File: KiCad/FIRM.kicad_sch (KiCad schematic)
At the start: 56 parts, among them J1 Conn_01x04_Pin, J2 USB_A, J3 Micro_SD_Card_Det2, Q1 AO3401A, U1 STM32F405RGTx, U2 LM2596S-3.3, U6 AP2112K-3.3, U7 W25Q128JVS, X2 32.768khz, Y1 12mhz

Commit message: test
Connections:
- net USB_D+ is gone; now on net VBUS: J2.3 (D+), U1.45 (PA12)
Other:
- moved on the sheet: C22, C23, C24, D1, Q1, R8, R9, U6

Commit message: update with drive
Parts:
- removed J2: USB_A, symbol Connector:USB_A
- removed U2: LM2596S-3.3, Package_TO_SOT_SMD:TO-263-5_TabPin3, symbol Regulator_Switching:LM2596S-3.3
- added J5: USB_C_Receptacle_USB2.0_16P, symbol Connector:USB_C_Receptacle_USB2.0_16P
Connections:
- net MISO is gone; now on net MISO2: U5.5 (SDO)
- net MOSI is gone; now on net MOSI2: U5.4 (SDI)
- net GND: now also J5.A1 (GND), J5.A12 (GND), J5.B1 (GND), J5.B12 (GND), J5.S1 (SHIELD)
- net USB_D-: now also J5.A7 (D-), J5.B7 (D-)
- net VBUS: now also J5.A4 (VBUS), J5.A9 (VBUS), J5.B4 (VBUS), J5.B9 (VBUS); no longer U1.45 (PA12)
- new net USB_D+: J5.A6 (D+), J5.B6 (D+), U1.45 (PA12)
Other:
- moved on the sheet: C22, C23, C24, D1, Q1, R8, R9, U6

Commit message: connector jst
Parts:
- added D5: LED, symbol Device:LED
- added R15: 2k2, symbol Device:R_Small
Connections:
- net +3.3V: now also R15.2
- net GND: now also D5.1 (K); no longer J1.3 (Pin_3), U1.49 (PA14)
- new net: D5.2 (A), R15.1
- new net SWCLK: J1.3 (Pin_3), U1.49 (PA14)
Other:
- moved on the sheet: J1

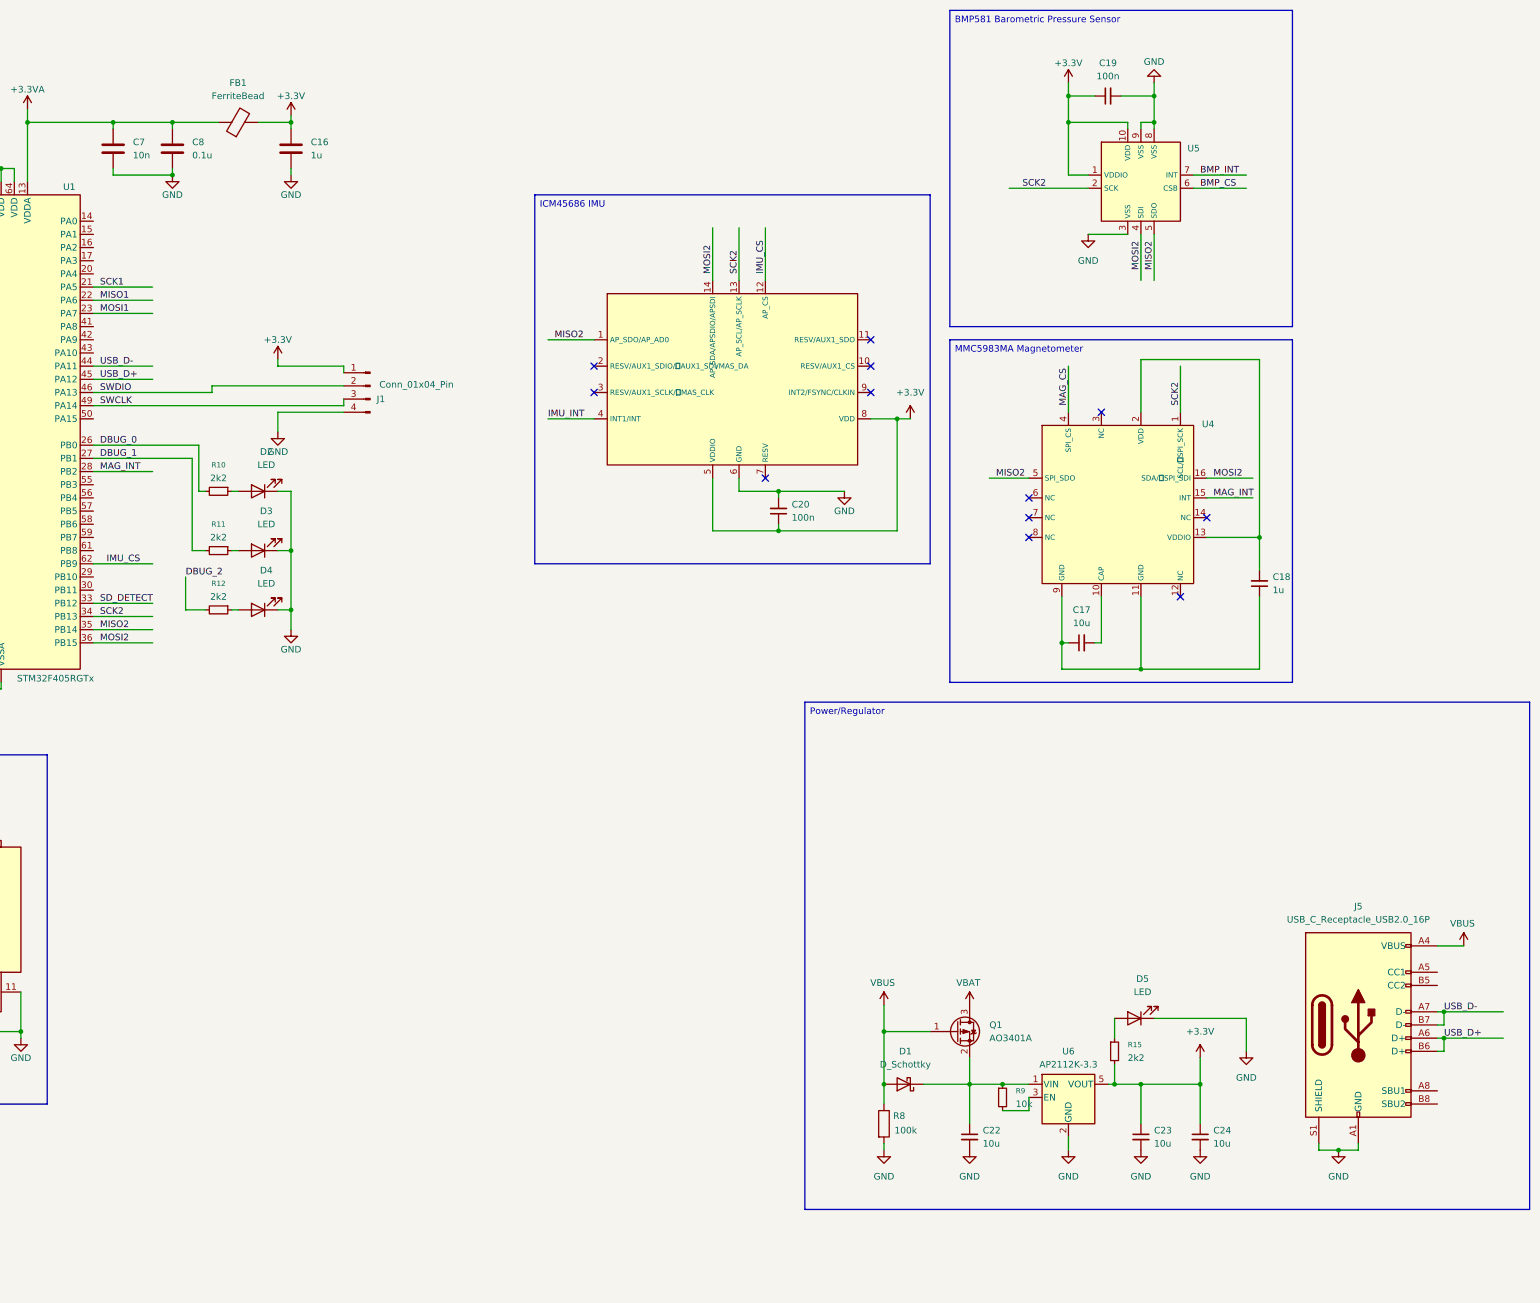
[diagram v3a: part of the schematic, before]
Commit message: Sensors Power/Decoupling and IMU/MMC Footprints
Fixed ICM, BMP, and MMC's power and decoupling. Added footprints for the MMC and ICM
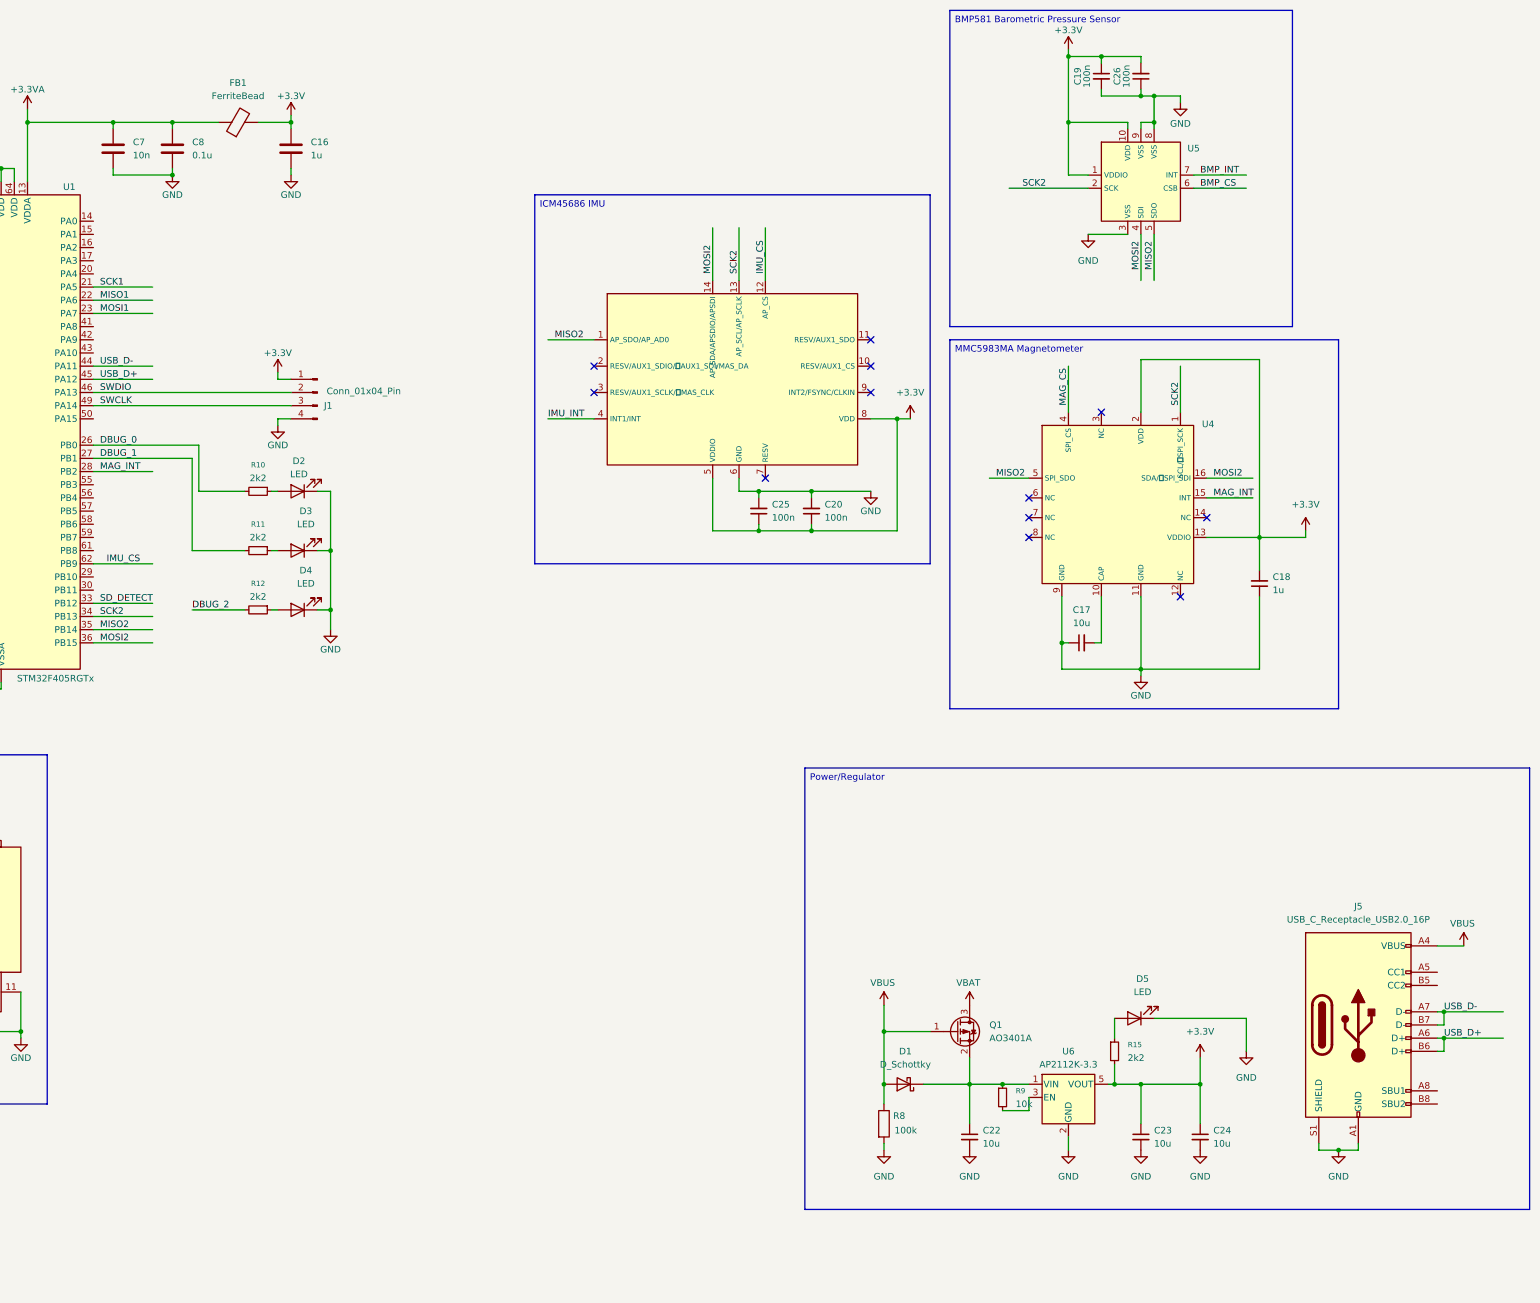
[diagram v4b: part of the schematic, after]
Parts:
- added C25, C26: 100n, symbol Device:C_Small
- U3: footprint Custom Components:ICM-45686 -> ICM-45686:IC_ICM-45686
- U4: footprint Custom Components:MMC5983MA -> MMC5983MA:PQFN50P300X300X100-16N
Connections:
- net +3.3V: now also C18.2, U4.13 (VDDIO), U4.2 (VDD), C25.1, C26.2
- net GND: now also C17.1, C18.1, U4.11 (GND), U4.9 (GND), C25.2, C26.1
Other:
- moved on the sheet: C19, C20, D2, D3, D4, J1, R10, R11, R12

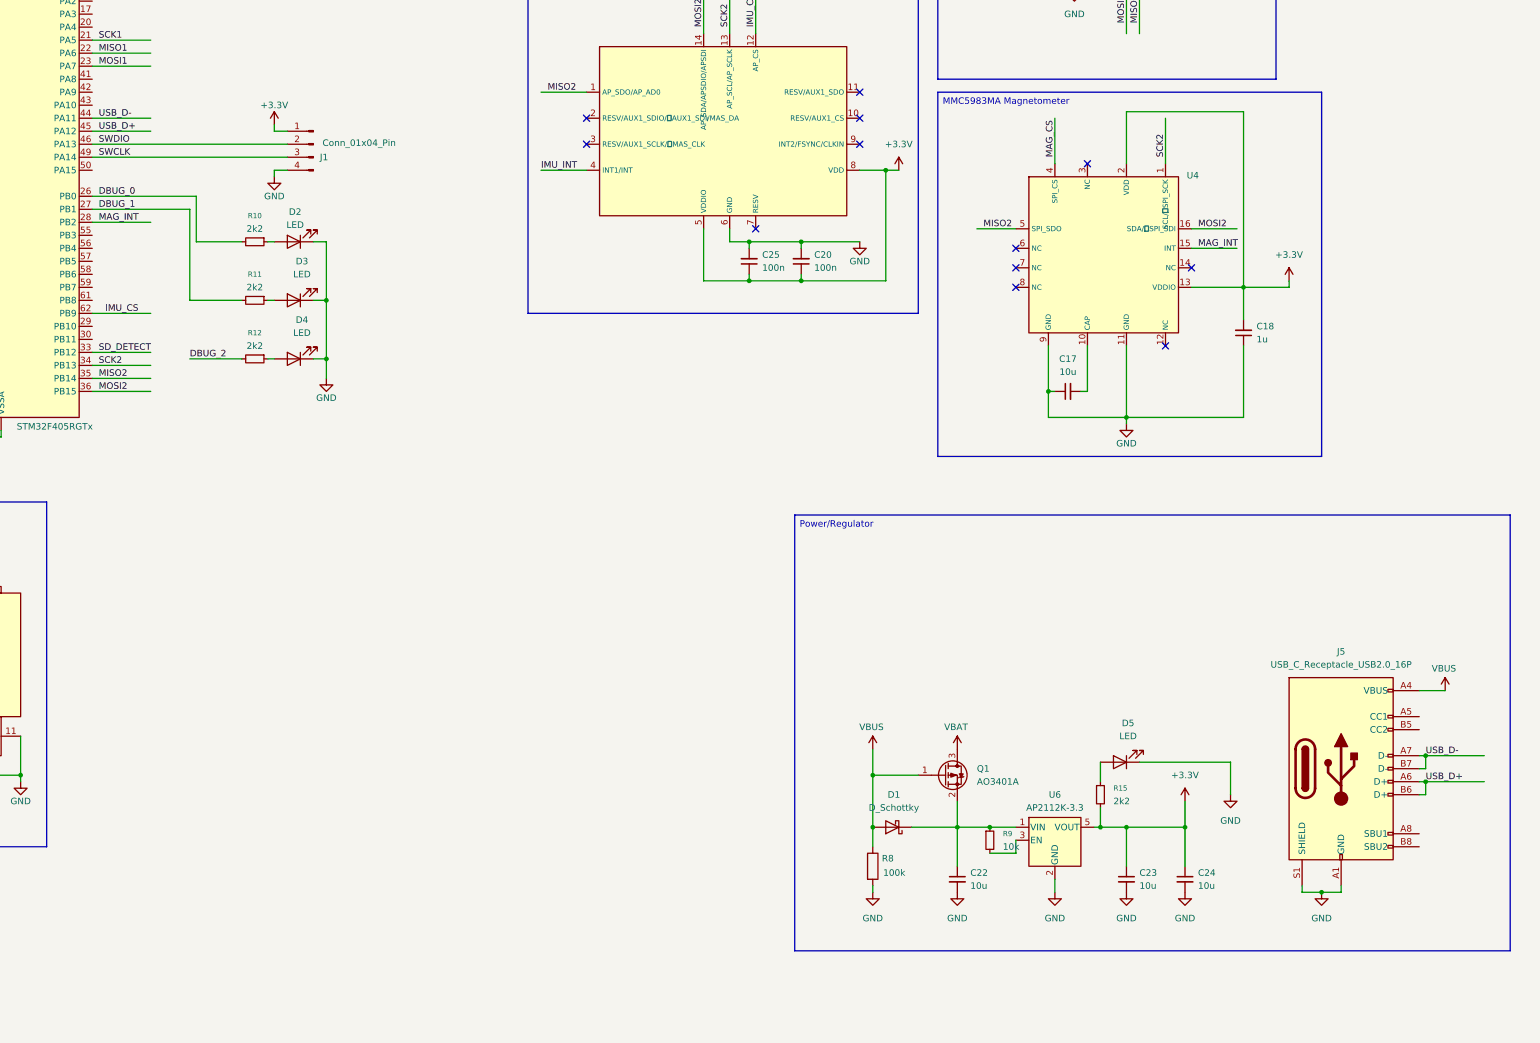
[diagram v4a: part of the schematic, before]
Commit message: Solder jump pads for the magnetometer
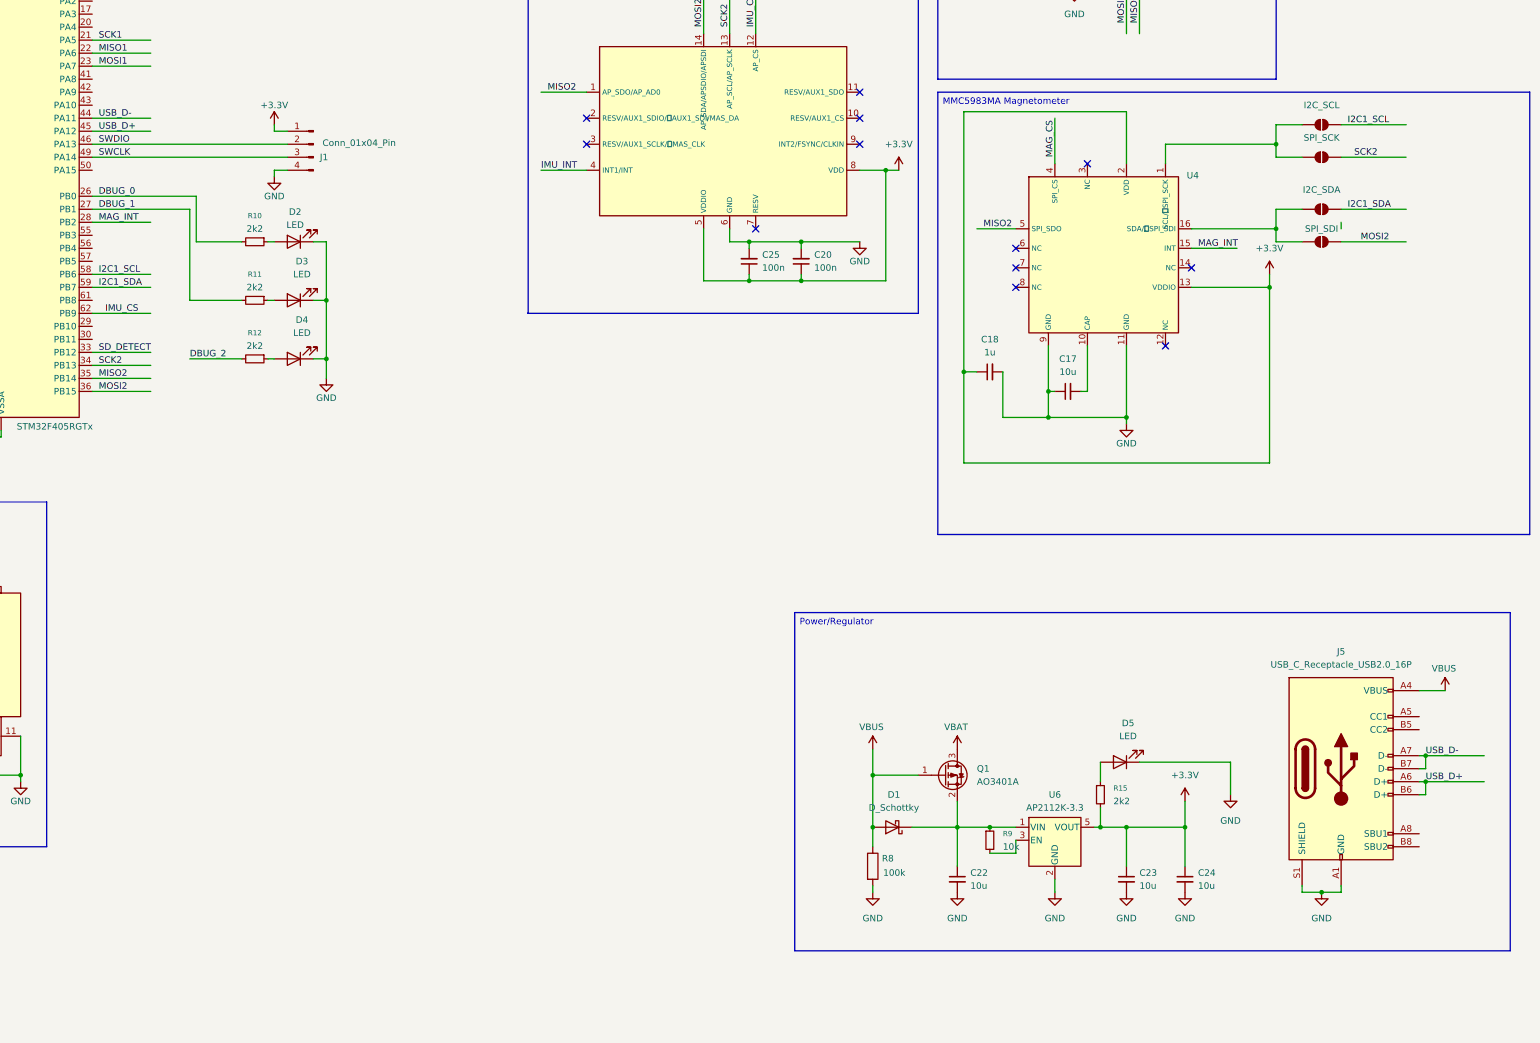
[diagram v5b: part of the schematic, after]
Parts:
- added JP1: I2C_SDA, symbol Jumper:SolderJumper_2_Open
- added JP2: SPI_SDI, symbol Jumper:SolderJumper_2_Open
- added JP3: I2C_SCL, symbol Jumper:SolderJumper_2_Open
- added JP4: SPI_SCK, symbol Jumper:SolderJumper_2_Open
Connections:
- net +3.3V: now also C18.1; no longer C18.2
- net GND: now also C18.2; no longer C18.1
- net MOSI2: now also JP2.2 (B); no longer U4.16 (SDA/ SPI_SDI)
- net SCK2: now also JP4.2 (B); no longer U4.1 (SCL/ SPI_SCK)
- net I2C1_SCL: now reaches U1.58 (PB6)
- net I2C1_SCL: now also JP3.2 (B)
- net I2C1_SDA: now reaches U1.59 (PB7)
- net I2C1_SDA: now also JP1.2 (B)
- new net: JP1.1 (A), JP2.1 (A), U4.16 (SDA/ SPI_SDI)
- new net: JP3.1 (A), JP4.1 (A), U4.1 (SCL/ SPI_SCK)
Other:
- moved on the sheet: C18
